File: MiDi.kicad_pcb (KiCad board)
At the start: 2 copper layers, 36.8 x 25.4 mm, 9 parts, among them J1 DIN-5_180degree, J2 Conn_01x06, U2 LTV-356T

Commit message: fix some drcs
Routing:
- net GND: vias 2 -> 1
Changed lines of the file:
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@@
     (effects (font (size 1 1) (thickness 0.15)) (justify left bottom))
   )
+  (segment (start 168.91 129.54) (end 168.91 128.27) (width 0.5) (layer "F.Cu") (net 1))
   (segment (start 169.57 125.07) (end 169.57 126.975) (width 0.5) (layer "F.Cu") (net 1))
   (segment (start 177.8 137.16) (end 177.8 130.445) (width 0.5) (layer "F.Cu") (net 1))
@@
   (segment (start 168.275 130.175) (end 169.765 130.175) (width 0.5) (layer "F.Cu") (net 1))
   (segment (start 166.45 132) (end 167.64 130.81) (width 0.5) (layer "F.Cu") (net 1))
-  (segment (start 167.64 130.81) (end 169.57 128.88) (width 0.5) (layer "F.Cu") (net 1))
   (segment (start 171.815 124.46) (end 170.18 124.46) (width 0.5) (layer "F.Cu") (net 1))
-  (segment (start 169.57 128.88) (end 169.57 126.975) (width 0.5) (layer "F.Cu") (net 1))
   (segment (start 177.8 130.445) (end 171.815 124.46) (width 0.5) (layer "F.Cu") (net 1))
   (segment (start 167.64 130.81) (end 168.275 130.175) (width 0.5) (layer "F.Cu") (net 1))
+  (segment (start 169.57 127.61) (end 169.57 126.975) (width 0.5) (layer "F.Cu") (net 1))
+  (segment (start 168.91 128.27) (end 169.57 127.61) (width 0.5) (layer "F.Cu") (net 1))
   (segment (start 170.18 124.46) (end 169.57 125.07) (width 0.5) (layer "F.Cu") (net 1))
+  (segment (start 167.64 130.81) (end 168.91 129.54) (width 0.5) (layer "F.Cu") (net 1))
   (segment (start 172.72 133.795) (end 171.64 132.715) (width 0.5) (layer "F.Cu") (net 2))
   (segment (start 172.11 126.975) (end 172.11 129.93) (width 0.5) (layer "F.Cu") (net 2))
@@
   (segment (start 178.689 122.936) (end 178.435 123.19) (width 0.5) (layer "F.Cu") (net 4))
   (via (at 170.815 128.905) (size 0.8) (drill 0.4) (layers "F.Cu" "B.Cu") (free) (net 4))
-  (via (at 170.815 127) (size 0.8) (drill 0.4) (layers "F.Cu" "B.Cu") (free) (net 4))
   (segment (start 170.77 122.555) (end 170.899244 122.555) (width 0.5) (layer "F.Cu") (net 5))
   (segment (start 178.499501 130.155257) (end 178.499501 130.620501) (width 0.5) (layer "F.Cu") (net 5))

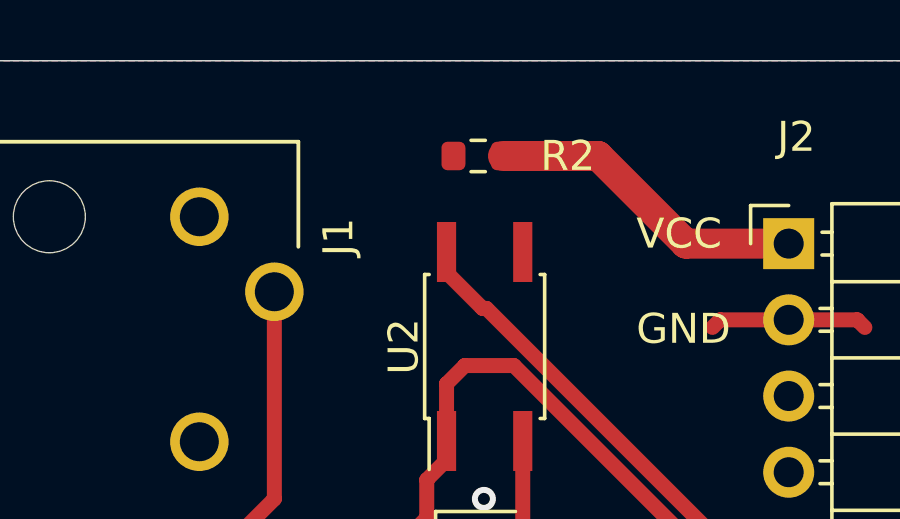
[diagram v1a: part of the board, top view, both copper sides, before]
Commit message: add v1 QR code
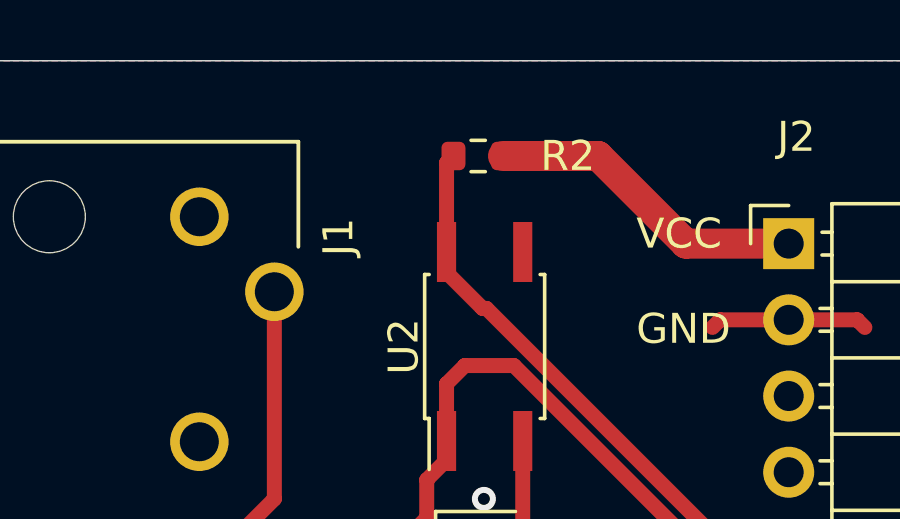
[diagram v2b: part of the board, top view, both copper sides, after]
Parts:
- added G***: LOGO, QR_Codes:V1_0QR, B.Cu at (156.2, 126.4)
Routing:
- net /Rx: track 17.2 -> 20.5 mm
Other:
- board text added: "Midi PMOD Rev 1.0 Copyright 2023 Tad Truex (tad@dartmouth.edu)"
- board text removed: "Midi PMOD Rev 1.0 Copyright 2023 Tad Truex (tadtruex@gmail.com) tinyurl.com/yc3v98x2"

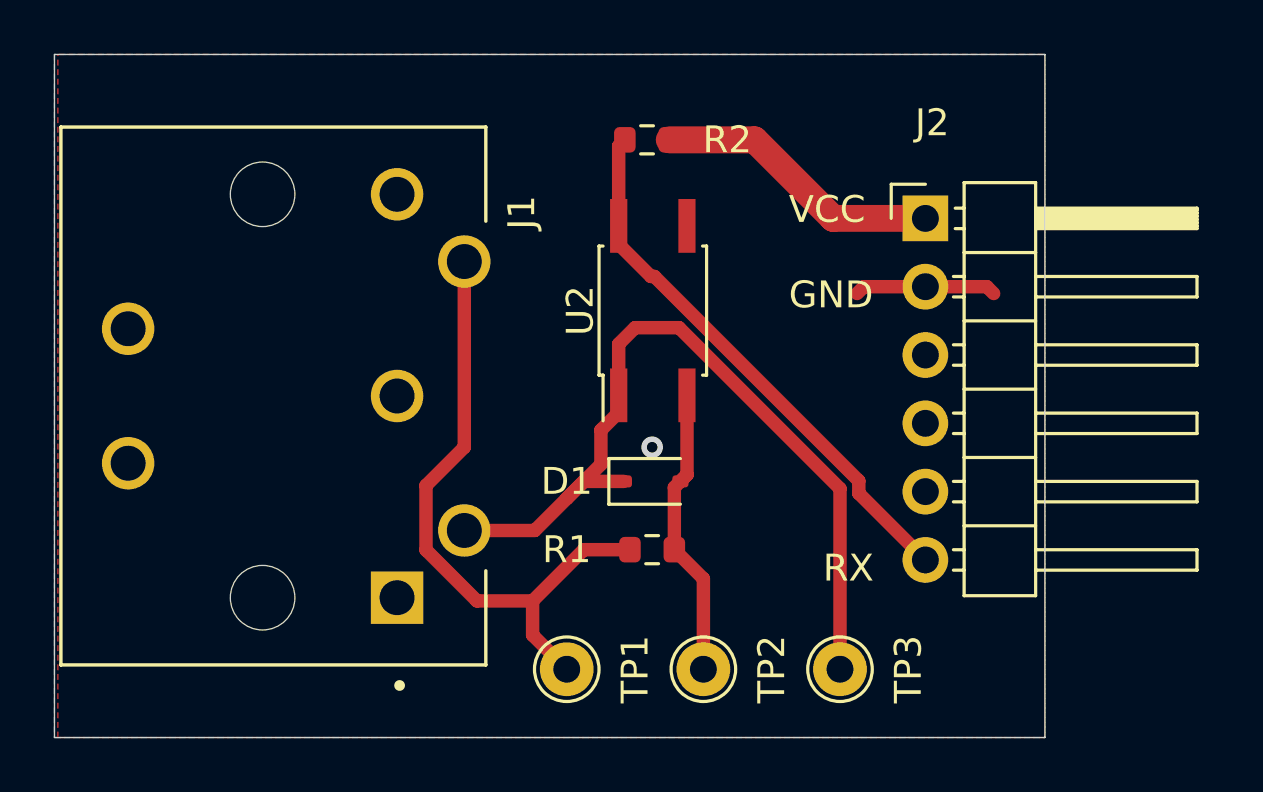
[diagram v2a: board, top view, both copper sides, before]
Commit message: V1.1
ChangeList

1) Reduce width to 0.8"
2) Reduce TP size (to 0.5mm) move inside edge cut
3) Move J2 closer to edge cut
4) Change Diode footprint to 603.  Old ?SMD_323? was too prone to
	tombstoning
5) Change QR Code.
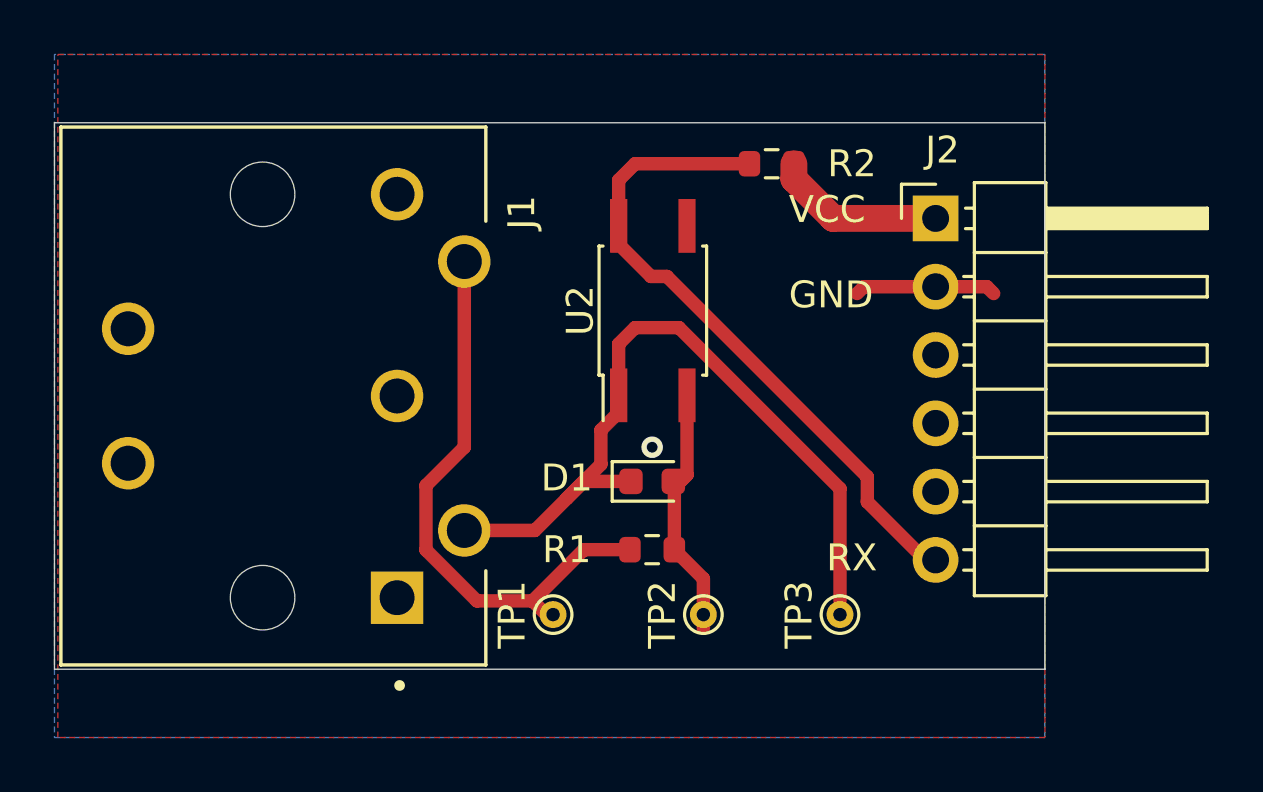
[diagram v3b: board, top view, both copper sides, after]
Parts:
- removed the G*** at (156.2, 126.4)
- added G***: LOGO, QR_Codes:Midi_V1_1_QR, B.Cu at (156.5, 126.5)
- D1: footprint Diode_SMD:D_SOD-323 -> Diode_SMD:D_0603_1608Metric
- TP1, TP2, TP3: footprint TestPoint:TestPoint_THTPad_D2.0mm_Drill1.0mm -> TestPoint:TestPoint_THTPad_D1.0mm_Drill0.5mm
- moved R2 4.72 mm to (175.3, 118.4)
- moved TP1 2.09 mm to (167.1, 135.1)
- moved TP2 2.03 mm to (172.7, 135.1)
- moved TP3 2.03 mm to (177.8, 135.1)
- moved J2 0.38 mm to (181.4, 120.4)
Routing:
- net +3.3V: track 10.7 -> 6.07 mm
- net /Rx: track 20.5 -> 24.3 mm
- net Net-(D1-K): track 30.9 -> 28.4 mm
- net Net-(J1-Pad5): track 23.5 -> 21.4 mm
- net Net-(D1-A): track 11.2 -> 9.65 mm
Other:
- board size 36.8 x 25.4 mm -> 36.8 x 20.3 mm
- board text added: "Midi PMOD Rev 1.1 Copyright 2023 Tad Truex (tad@dartmouth.edu)"
- board text removed: "Midi PMOD Rev 1.0 Copyright 2023 Tad Truex (tad@dartmouth.edu)"

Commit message: Modify DIN5 footprint file to work with both prevalent styles of DIN5 connector
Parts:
- G***: footprint QR_Codes:Midi_V1_1_QR -> QR_Codes:Midi_V1_1a_QR
- J1: footprint StockedComponents:CUI_SDS-50J -> StockedComponents:DIN5_MIDI
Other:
- board text added: "Midi PMOD Rev 1.1a Copyright 2023 Tad Truex (tad@dartmouth.edu)"
- board text removed: "Midi PMOD Rev 1.1 Copyright 2023 Tad Truex (tad@dartmouth.edu)"
